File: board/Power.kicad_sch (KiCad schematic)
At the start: 26 parts, among them J37 PWR MODE, J7 Front Panel, J8 ATX-24, Q1 2N7000, U36 DS1813-5, U78 CD40106B, U79 CD4013B, U80 L79L05

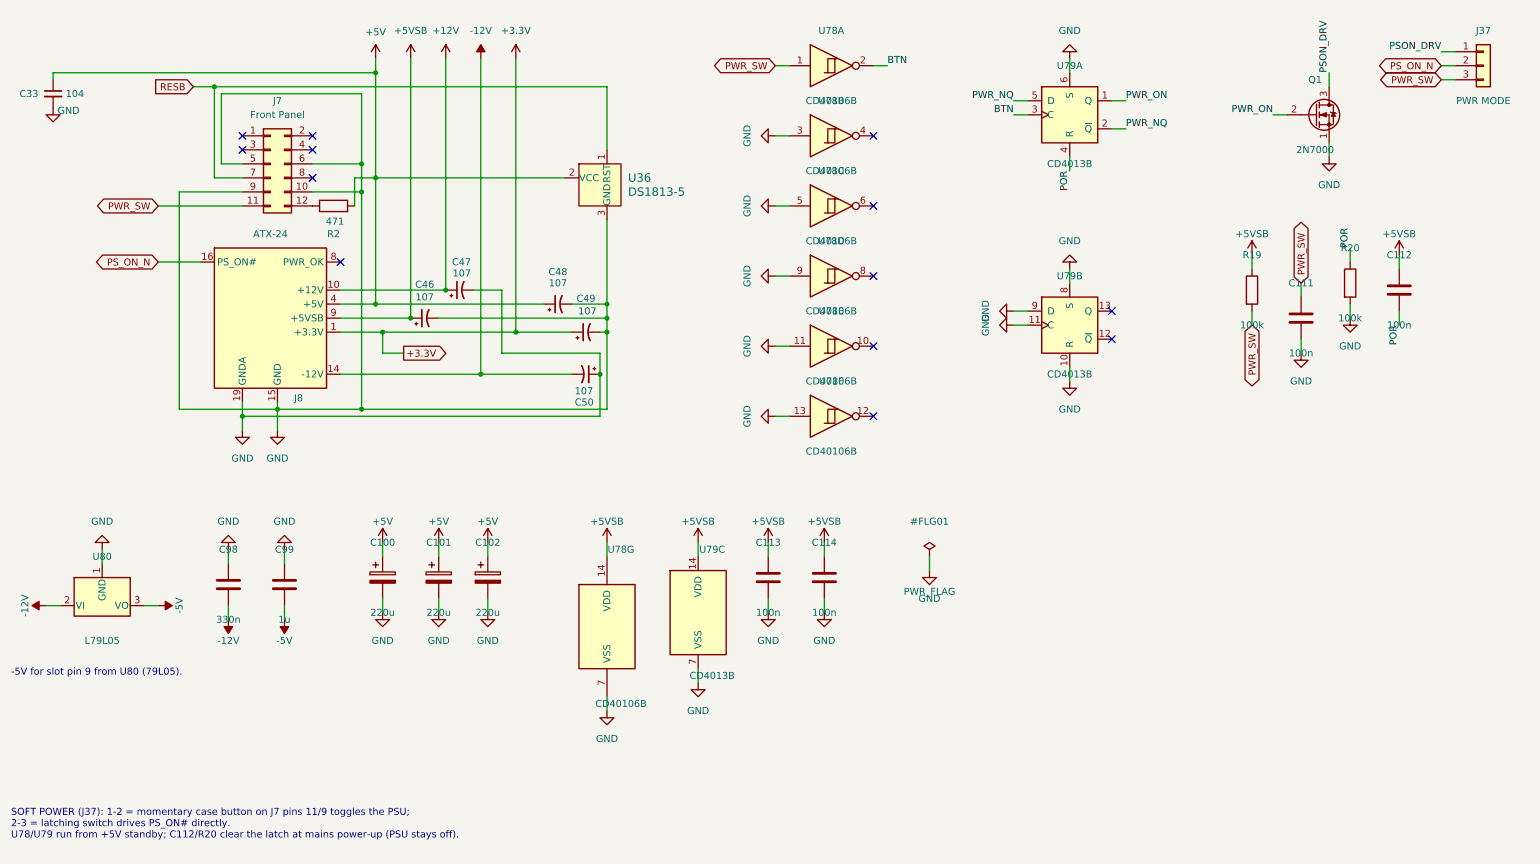
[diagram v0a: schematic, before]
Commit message: V2.0: slot pin 9 to +3.3V, amplifier on +5V
Slots:
- Pin 9 on all six slots now carries +3.3V instead of -5V, so each card
  gets two 3.3 V pins (9 and 24); no existing card used -5V
- Slot connector symbol pin 9 renamed +3.3V; slot bus rules note updated
- Removed U80 (79L05), C98 and C99 from the Power sheet

Amplifier:
- U89 TDA2822M now runs from +5V through an RC filter (R32 1R, C122 1000u)
- Removed U90 (L7809), C124 and C125
- R26/R27 470k (same volume range at 5 V); R30/R31 2.2R (same footprint)
- PWR_FLAG on the new AMP_5V net; sheet note updated

PCB updated from the schematic.

Also tidied overlapping text on the Power sheet (U78/U79 labels, PWR_FLAG,
R19/C111/R20/C112); connectivity unchanged.

Co-Authored-By: Claude Opus 5.5 <noreply@anthropic.com>
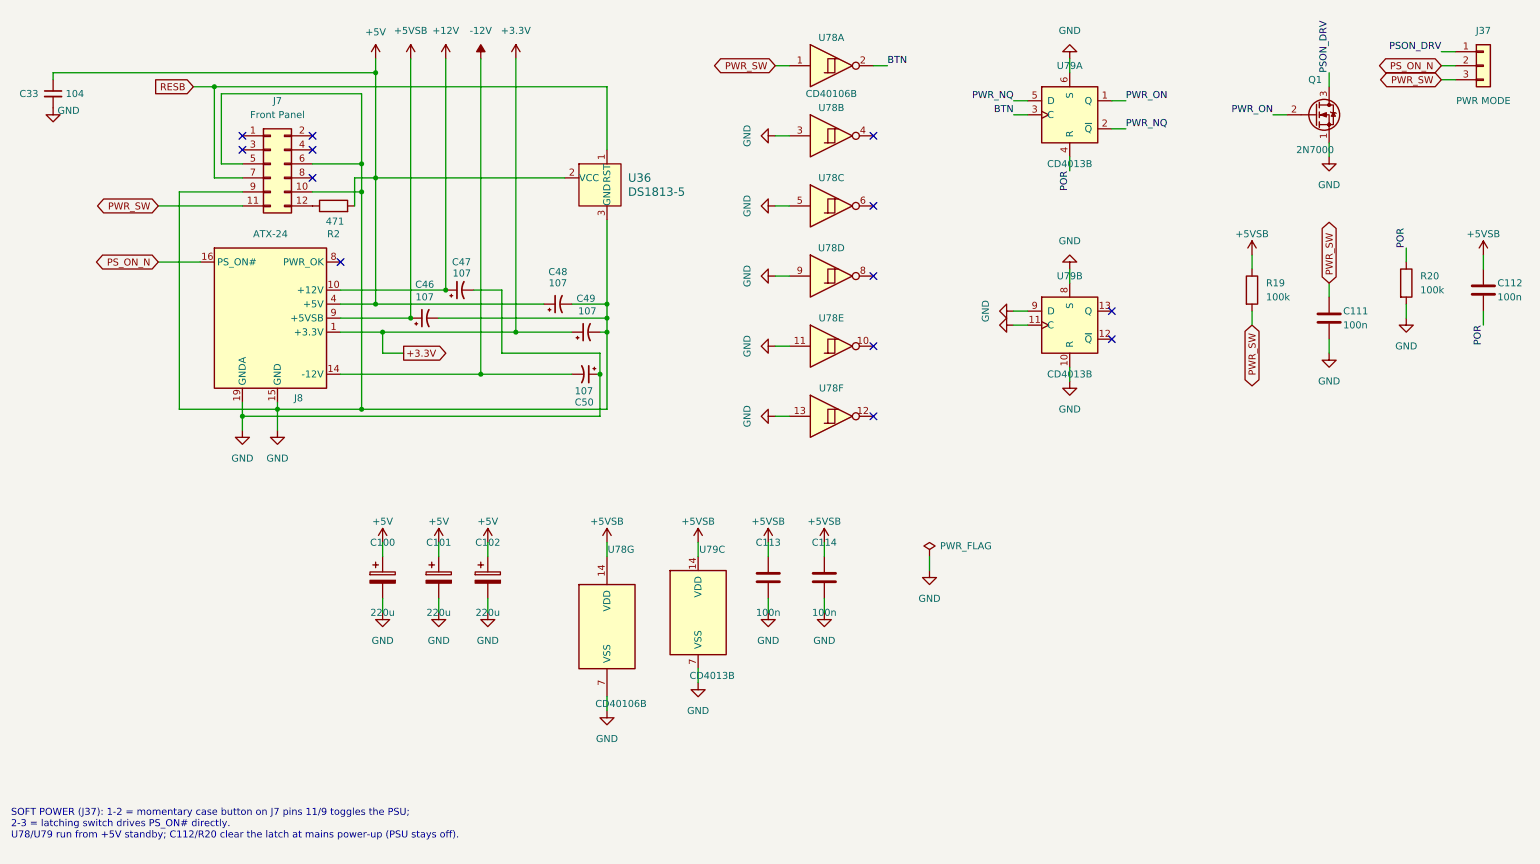
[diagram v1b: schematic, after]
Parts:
- removed C98: 330n, Capacitor_THT:C_Disc_D5.0mm_W2.5mm_P5.00mm, symbol Device:C
- removed C99: 1u, Capacitor_THT:C_Disc_D5.0mm_W2.5mm_P5.00mm, symbol Device:C
- removed U80: L79L05, Package_TO_SOT_THT:TO-92_Inline, symbol Regulator_Linear:L79L05_TO92
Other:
- note removed: "-5V for slot pin 9 from U80 (79L05)."
- title: Power: ATX, Front Panel, Reset, Soft Power, -5V -> Power: ATX, Front Panel, Reset, Soft Power
- moved on the sheet: C111, C112, R20

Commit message: V2.0: consolidate parts (239 -> 216), GAL C rev 02
No change in function:
- U9 74F08 removed: GAL C (U88) rev 02 makes the CPU phi0 (P_PHI0 = PHI2
  held low while DMAB_S is low); its decoupling cap C14 removed
- U34 74ACT14 removed: the two clock buffers use spare U19 74F240 gates
- U60 + U61 (2 x CY7C192 vector RAM) replaced by one AS7C256B-15
  (32K x 8, 15 ns); the IRQ sheet's D[0..7] bus is gone
- Crystal oscillators (U75 74HCU04, Y1, Y2, R1, R6-R8, C43, C44, C96,
  C97) replaced by canned oscillators X1 (14.31818 MHz), X2 (1.8432 MHz)
- Soft power: CD40106 -> 74HC14, CD4013 -> 74HC74 (active-low set/reset,
  power-on reset network inverted); a spare 74HC14 gate drives PS_ON#,
  so Q1 is removed
- R10-R13 -> RN6 (4 x 10k, SIP-5); R9, R21-R24 -> RN7 (5 x 33R isolated,
  SIP-10)
- C100-C102 (3 x 220u) -> C100 680u
- Clocks and Power sheet notes updated; PLD README updated

GAL C rev 02 verified against rev 01 over 200,000 clock edges.
PCB updated from the schematic (adds RN6, RN7, X1, X2 and the speakers
LS1/LS2). Also includes KiCad's re-save of the schematic sheets.

Co-Authored-By: Claude Opus 5.5 <noreply@anthropic.com>
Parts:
- removed C101, C102: 220u, Capacitor_THT:CP_Radial_D8.0mm_P3.50mm, symbol Device:C_Polarized
- removed Q1: 2N7000, Package_TO_SOT_THT:TO-92_Inline, symbol Transistor_FET:2N7000
- C100: value 220u -> 680u; footprint Capacitor_THT:CP_Radial_D8.0mm_P3.50mm -> Capacitor_THT:CP_Radial_D10.0mm_P5.00mm
- U78: value CD40106B -> 74HC14; symbol 4xxx:40106 -> 74xx:74HC14
- U79: value CD4013B -> 74HC74; symbol 4xxx:4013 -> 74xx:74HC74
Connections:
- net +5VSB: now also R20.2, U79.10 (~{S}), U79.13 (~{R}), U79.4 (~{S}); no longer C112.1
- net GND: now also C112.1, U79.12 (D); no longer R20.2, U78.3, U79.10 (R), U79.6 (S), U79.8 (S), U79.9 (D)
- net POR: now also U79.1 (~{R}); no longer U79.4 (R)
- net PSON_DRV: now also U78.4
- net PWR_NQ: now also U79.6 (~{Q}); no longer U79.5 (D)
- net PWR_ON: now also U78.3, U79.5 (Q); no longer U79.1 (Q)
- no-connect marks 13 -> 12
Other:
- note added: "SOFT POWER (J37): 1-2 = momentary case button on J7 pins 11/9 toggles the PSU; 2-3 = latching switch drives PS_ON# directly. U78 (74HC14) and U79 (74HC74) run from +5V standby. R20/C112 hold U79 cleared at mains power-up (PSU stays off). U78B drives PS_ON# (push-pull) through J37 1-2."
- note removed: "SOFT POWER (J37): 1-2 = momentary case button on J7 pins 11/9 toggles the PSU; 2-3 = latching switch drives PS_ON# directly. U78/U79 run from +5V standby; C112/R20 clear the latch at mains power-up (PSU stays off)."
